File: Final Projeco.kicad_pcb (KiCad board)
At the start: 2 copper layers, 25 x 45 mm, 16 parts, among them U1 ESP32-S3, U2 GT-USB-7004N, U3 NCP167BMX330TBG, X1 TZ1269D

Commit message: Fixed all the traces to connect to each other :-|
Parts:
- added C8: 1uF, Capacitor_SMD:C_0402_1005Metric, F.Cu at (49.5, 56.5)
- added C9: 0.1uF, Capacitor_SMD:C_0402_1005Metric, F.Cu at (49.5, 59.0)
- added D1: SD103AWS_C5345966, jlc:SOD-323_L1.7-W1.3-LS2.5-RD, F.Cu at (35.2, 27.5)
- added D2: SD103AWS_C5345966, jlc:SOD-323_L1.7-W1.3-LS2.5-RD, F.Cu at (46.5, 24.7)
- added D3: SD103AWS_C5345966, jlc:SOD-323_L1.7-W1.3-LS2.5-RD, F.Cu at (44.5, 24.7)
- added R5: 100K, Resistor_SMD:R_0402_1005Metric, F.Cu at (47.0, 59.0)
- added U4: LY68L6400SLIT, jlc:SOP-8_L4.9-W3.9-P1.27-LS6.0-BL, F.Cu at (37.1, 33.7)
- added U5: PTS830GG140SMTRLFS, jlc:KEY-SMD_4P-L3.1-W2.6_PTS830GG140SMTRLFS, F.Cu at (43.9, 53.8)
- added U6: PTS830GG140SMTRLFS, jlc:KEY-SMD_4P-L3.1-W2.6_PTS830GG140SMTRLFS, F.Cu at (48.6, 53.8)
- added U7: 220S-2*16P_H=8_5MM_Ytype_L=3_0MM_PBT, jlc:HDR-TH_32P-P2.54-V-F-R2-C16-S2.54, F.Cu at (29.8, 36.6)
- C4: value C -> 1u
- moved U3 27.5 mm to (44.0, 17.0), turned to 90 degrees
- moved R1 18.3 mm to (41.0, 49.5), turned to 180 degrees
- moved U1 17.5 mm to (44.2, 33.9), turned to 180 degrees
- moved C7 13.3 mm to (47.0, 56.5), turned to 180 degrees
- moved X1 10.6 mm to (46.0, 40.1), turned to -90 degrees
- moved R2 10.5 mm to (40.9, 43.6)
- moved C2 10.5 mm to (38.0, 43.6)
- moved C3 10.5 mm to (38.0, 45.5)
- moved C4 10.5 mm to (38.0, 47.5)
- moved C5 10.5 mm to (38.0, 49.5)
- moved C6 10.5 mm to (38.0, 51.4)
- moved R3 10.5 mm to (40.9, 45.6), turned to 180 degrees
- moved R4 10.5 mm to (40.9, 47.6)
- moved C1 10.3 mm to (41.0, 41.0)
- moved U2 7.53 mm to (38.1, 21.9), turned to 180 degrees
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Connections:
- C1 pad 2: Net-(C1-Pad2) -> /XTAL_P
- C2 pad 1: Net-(C2-Pad1) -> /XTAL_N
- C3 pad 1: Net-(C3-Pad1) -> /RESET
- C5 pad 1: Net-(U3-OUT) -> VDD3P3
- C6 pad 1: Net-(U3-EN) -> /VBUS
- R1 pad 2: Net-(C3-Pad1) -> /RESET
- R2 pad 1: Net-(U2-CC2) -> /VBUS
- R3 pad 1: Net-(U2-CC1) -> /VBUS
- U1 pad 10: unconnected-(U1-GPIO5/ADC1_CH4-Pad10) -> /GPIO5
- U1 pad 11: unconnected-(U1-GPIO6/ADC1_CH5-Pad11) -> /GPIO6
- U1 pad 12: unconnected-(U1-GPIO7/ADC1_CH6-Pad12) -> /GPIO7
- U1 pad 13: unconnected-(U1-GPIO8/ADC1_CH7-Pad13) -> /GPIO8
- U1 pad 14: unconnected-(U1-GPIO9/ADC1_CH8-Pad14) -> /GPIO9'
- U1 pad 15: unconnected-(U1-GPIO10/ADC1_CH9-Pad15) -> /GPIO10
- U1 pad 16: unconnected-(U1-GPIO11/ADC2_CH0-Pad16) -> /GPIO11
- U1 pad 17: unconnected-(U1-GPIO12/ADC2_CH1-Pad17) -> /GPIO12
- U1 pad 18: unconnected-(U1-GPIO13/ADC2_CH2-Pad18) -> /GPIO13
- U1 pad 19: unconnected-(U1-GPIO14/ADC2_CH3-Pad19) -> /GPIO14
- U1 pad 20: unconnected-(U1-VDD3P3_RTC-Pad20) -> VDD3P3
- U1 pad 23: unconnected-(U1-GPIO17/ADC2_CH6-Pad23) -> /GPIO!7
- U1 pad 24: unconnected-(U1-GPIO18/ADC2_CH7-Pad24) -> /GPIO18
- U1 pad 25: unconnected-(U1-GPIO19/USB_D-/ADC2_CH8-Pad25) -> /USB_D+
- U1 pad 26: unconnected-(U1-GPIO20/USB_D+/ADC2_CH9-Pad26) -> /USB_D-
- U1 pad 27: unconnected-(U1-GPIO21-Pad27) -> /GPIO21
- U1 pad 28: unconnected-(U1-SPI_CS1/GPIO26-Pad28) -> /SPICS1
- U1 pad 29: unconnected-(U1-VDD_SPI-Pad29) -> VDD3P3
- U1 pad 30: unconnected-(U1-SPIHD/GPIO27-Pad30) -> /SPIHD
- U1 pad 31: unconnected-(U1-SPIWP/GPIO28-Pad31) -> /SPIWP
- U1 pad 33: unconnected-(U1-SPICLK/GPIO30-Pad33) -> /SPICLK
- U1 pad 34: unconnected-(U1-SPIQ/GPIO31-Pad34) -> /SPIQ
- U1 pad 35: unconnected-(U1-SPID/GPIO32-Pad35) -> /SPID
- U1 pad 4: unconnected-(U1-CHIP_PU/RESET-Pad4) -> /RESET
- U1 pad 43: unconnected-(U1-GPIO38-Pad43) -> /GPIO38
- U1 pad 46: unconnected-(U1-VDD3P3_CPU-Pad46) -> VDD3P3
- U1 pad 5: unconnected-(U1-GPIO0/BOOT-Pad5) -> /GPIO0/BOOT
- U1 pad 51: unconnected-(U1-GPIO45-Pad51) -> /GPIO45
- U1 pad 52: unconnected-(U1-GPIO46-Pad52) -> /GPIO46
- U1 pad 53: unconnected-(U1-XTAL_N-Pad53) -> /XTAL_P
- U1 pad 54: unconnected-(U1-XTAL_P-Pad54) -> /XTAL_N
- U1 pad 55: Net-(U1-VDDA-Pad55) -> VDD3P3
- U1 pad 56: Net-(U1-VDDA-Pad55) -> VDD3P3
- U1 pad 6: unconnected-(U1-GPIO1/ADC1_CH0-Pad6) -> /GPIO1
- U1 pad 7: unconnected-(U1-GPIO2/ADC1_CH1-Pad7) -> /GPIO2
- U1 pad 8: unconnected-(U1-GPIO3/ADC1_CH2-Pad8) -> /GPIO3
- U1 pad 9: unconnected-(U1-GPIO4/ADC1_CH3-Pad9) -> /GPIO4
- U2 pad 1: unconnected-(U2-SHELL-Pad1) -> GND
- U2 pad A4B9: Net-(U2-CC1) -> /VBUS
- U2 pad A5: Net-(U2-CC1) -> /VBUS
- U2 pad A6: unconnected-(U2-DP1-PadA6) -> /USB_D+
- U2 pad A7: unconnected-(U2-DN1-PadA7) -> /USB_D-
- U2 pad B4A9: Net-(U2-CC2) -> /VBUS
- U2 pad B5: Net-(U2-CC2) -> /VBUS
- U2 pad B6: unconnected-(U2-DP2-PadB6) -> /USB_D+
- U2 pad B7: unconnected-(U2-DN2-PadB7) -> /USB_D-
- U3 pad 1: Net-(U3-OUT) -> VDD3P3
- U3 pad 3: Net-(U3-EN) -> /VBUS
- U3 pad 4: Net-(U3-EN) -> /VBUS
- X1 pad 1: Net-(C1-Pad2) -> /XTAL_P
- X1 pad 3: Net-(C2-Pad1) -> /XTAL_N

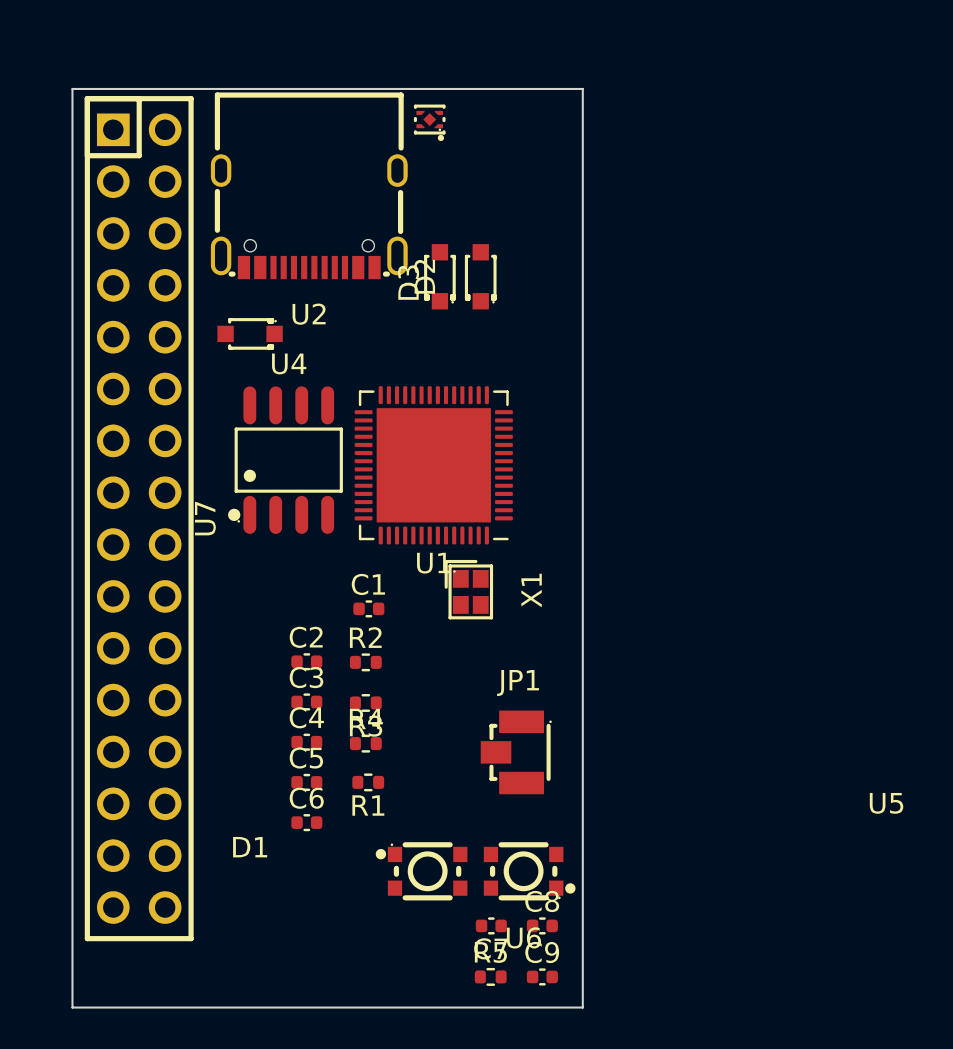
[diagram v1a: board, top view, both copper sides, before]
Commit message: Fixed some stuff
-added diff pair net rules
-added base net rules
-added zmatch net rules
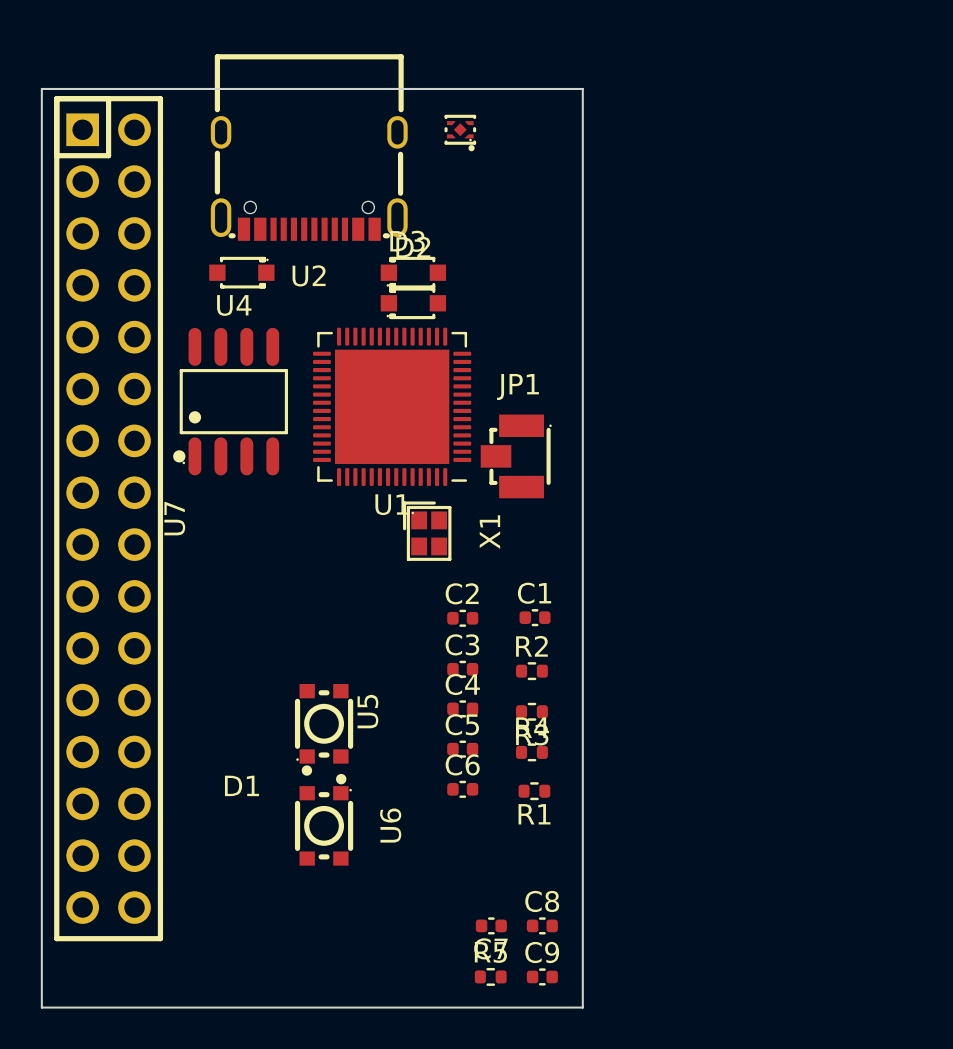
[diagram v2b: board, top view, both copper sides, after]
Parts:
- moved JP1 14.5 mm to (47.9, 33.5)
- moved U6 10.0 mm to (38.8, 51.6), turned to -90 degrees
- moved U5 8.83 mm to (38.8, 46.6), turned to 90 degrees
- moved R1 8.15 mm to (49.1, 49.9)
- moved R2 8.15 mm to (49.0, 44.0)
- moved R3 8.15 mm to (49.0, 46.0)
- moved R4 8.15 mm to (49.0, 48.0)
- moved C1 8.15 mm to (49.2, 41.4)
- moved C2 7.93 mm to (45.6, 41.4)
- moved C4 7.81 mm to (45.6, 45.9)
- moved C5 7.81 mm to (45.6, 47.8)
- moved C6 7.81 mm to (45.6, 49.8)
- moved C3 7.81 mm to (45.6, 43.9)
- moved U4 3.93 mm to (34.4, 30.8)
- moved D2 3.55 mm to (43.2, 26.0), turned to 0 degrees
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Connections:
- U1 pad 14: /GPIO9' -> /GPIO9
- U1 pad 23: /GPIO!7 -> /GPIO17
- U7 pad 11: unconnected-(U7-Pad11) -> /GPIO38
- U7 pad 12: /GPIO3 -> /GPIO4
- U7 pad 13: unconnected-(U7-Pad13) -> /GPIO45
- U7 pad 14: /GPIO4 -> /GPIO5
- U7 pad 15: unconnected-(U7-Pad15) -> /GPIO46
- U7 pad 16: /GPIO5 -> /GPIO6
- U7 pad 18: /GPIO6 -> /GPIO7
- U7 pad 20: /GPIO7 -> /GPIO8
- U7 pad 22: /GPIO8 -> /GPIO9
- U7 pad 24: /GPIO9' -> /GPIO10
- U7 pad 26: /GPIO10 -> /GPIO11
- U7 pad 28: /GPIO11 -> /GPIO12
- U7 pad 3: unconnected-(U7-Pad3) -> /GPIO14
- U7 pad 30: /GPIO12 -> /GPIO13
- U7 pad 31: unconnected-(U7-Pad31) -> VDD3P3
- U7 pad 32: /GPIO13 -> GND
- U7 pad 5: unconnected-(U7-Pad5) -> /GPIO17
- U7 pad 7: unconnected-(U7-Pad7) -> /GPIO18
- U7 pad 9: unconnected-(U7-Pad9) -> /GPIO21
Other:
- board size 25 x 45 mm -> 26.5 x 45 mm
- copper layers 2 -> 6

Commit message: Started Routing
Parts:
- C4: value 1u -> 1uF
- moved C6 30.2 mm to (43.9, 19.7)
- moved C5 28.3 mm to (48.6, 19.7), turned to 180 degrees
- moved R5 27.0 mm to (32.6, 36.2), turned to 90 degrees
- moved C9 25.0 mm to (33.3, 40.0)
- moved R3 24.6 mm to (47.0, 21.5), turned to -90 degrees
- moved R2 22.8 mm to (45.2, 21.5), turned to -90 degrees
- moved C8 22.0 mm to (33.3, 41.6)
- moved C4 20.3 mm to (48.4, 25.8)
- moved R1 13.7 mm to (37.5, 42.6)
- moved R4 10.3 mm to (40.2, 42.6)
- moved C3 9.56 mm to (38.1, 38.0)
- moved C1 9.32 mm to (40.5, 38.0)
- moved C7 7.32 mm to (41.6, 51.6), turned to 90 degrees
- moved D3 4.43 mm to (38.8, 25.0), turned to 180 degrees
- moved U3 3.20 mm to (48.7, 17.5)
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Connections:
- R1 pad 1: +3.3V -> VDD3P3
- R4 pad 1: +3.3V -> VDD3P3
- U1 pad 21: unconnected-(U1-GPIO15/ADC2_CH4/XTAL_32K_P-Pad21) -> /GPIO15
- U1 pad 22: unconnected-(U1-GPIO16/ADC2_CH5/XTAL_32K_N-Pad22) -> /GPIO16
- U1 pad 38: unconnected-(U1-GPIO33-Pad38) -> /GPIO33
- U1 pad 39: unconnected-(U1-GPIO34-Pad39) -> /GPIO34
- U1 pad 40: unconnected-(U1-GPIO35-Pad40) -> /GPIO35
- U1 pad 41: unconnected-(U1-GPIO36-Pad41) -> /GPIO36
- U1 pad 42: unconnected-(U1-GPIO37-Pad42) -> /GPIO37
- U7 pad 1: VDD3P3 -> /GPIO12
- U7 pad 10: /GPIO3 -> /GPIO2
- U7 pad 11: /GPIO38 -> /GPIO17
- U7 pad 12: /GPIO4 -> /GPIO3
- U7 pad 13: /GPIO45 -> /GPIO18
- U7 pad 14: /GPIO5 -> /GPIO4
- U7 pad 15: /GPIO46 -> /GPIO21
- U7 pad 16: /GPIO6 -> /GPIO5
- U7 pad 17: unconnected-(U7-Pad17) -> /GPIO38
- U7 pad 18: /GPIO7 -> /GPIO6
- U7 pad 19: unconnected-(U7-Pad19) -> /GPIO45
- U7 pad 20: /GPIO8 -> /GPIO7
- U7 pad 21: unconnected-(U7-Pad21) -> /GPIO46
- U7 pad 22: /GPIO9 -> /GPIO8
- U7 pad 23: unconnected-(U7-Pad23) -> /GPIO33
- U7 pad 24: /GPIO10 -> /GPIO9
- U7 pad 25: unconnected-(U7-Pad25) -> /GPIO34
- U7 pad 26: /GPIO11 -> /GPIO10
- U7 pad 27: unconnected-(U7-Pad27) -> /GPIO35
- U7 pad 28: /GPIO12 -> /GPIO11
- U7 pad 29: unconnected-(U7-Pad29) -> /GPIO36
- U7 pad 3: /GPIO14 -> /GPIO13
- U7 pad 30: /GPIO13 -> VDD3P3
- U7 pad 31: VDD3P3 -> /GPIO37
- U7 pad 4: /GPIO0/BOOT -> VDD3P3
- U7 pad 5: /GPIO17 -> /GPIO14
- U7 pad 6: /GPIO1 -> /GPIO0/BOOT
- U7 pad 7: /GPIO18 -> /GPIO15
- U7 pad 8: /GPIO2 -> /GPIO1
- U7 pad 9: /GPIO21 -> /GPIO16
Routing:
- net /VBUS: track 0.00 -> 29.0 mm
- net GND: track 0.00 -> 23.2 mm, vias 0 -> 19
- net VDD3P3: track 0.00 -> 11.0 mm, vias 0 -> 8
- net /USB_D+: track 0.00 -> 9.45 mm, vias 0 -> 2
- net /USB_D-: track 0.00 -> 9.03 mm
- net /XTAL_N: track 0.00 -> 7.91 mm
- net /XTAL_P: track 0.00 -> 6.53 mm
- net Net-(JP1-SIN): track 0.00 -> 1.90 mm
- net /RESET: track 0.00 -> 1.31 mm
- added copper zone on In1.Cu, net GND
- added copper zone on In2.Cu, net VDD3P3
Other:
- board text added: "William Schoon"

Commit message: stuff
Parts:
- added C10: 1uF, Capacitor_SMD:C_0402_1005Metric, F.Cu at (35.5, 36.3)
- added R6: 442k, Resistor_SMD:R_0402_1005Metric, F.Cu at (37.4, 36.3)
- C1, C2: value C -> 13pF
- C5, C6: value C -> 1uF
- moved C4 2.33 mm to (47.2, 27.8)
- moved U7 0.59 mm to (28.5, 37.1)
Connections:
- net Net-(U1-GND) renamed /GND_PIN
- U1 pad 37: unconnected-(U1-SPICLK_P/GPIO47-Pad37) -> /SPICLK_GPIO47
- U2 pad 2: unconnected-(U2-SHELL-Pad2) -> GND
- U2 pad 3: unconnected-(U2-SHELL-Pad3) -> GND
- U2 pad 4: unconnected-(U2-SHELL-Pad4) -> GND
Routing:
- net /GND_PIN: track 0.00 -> 5.96 mm
- net VDD3P3: track 11.0 -> 13.9 mm
- net /USB_D-: track 9.03 -> 9.92 mm
- net GND: track 23.2 -> 23.8 mm

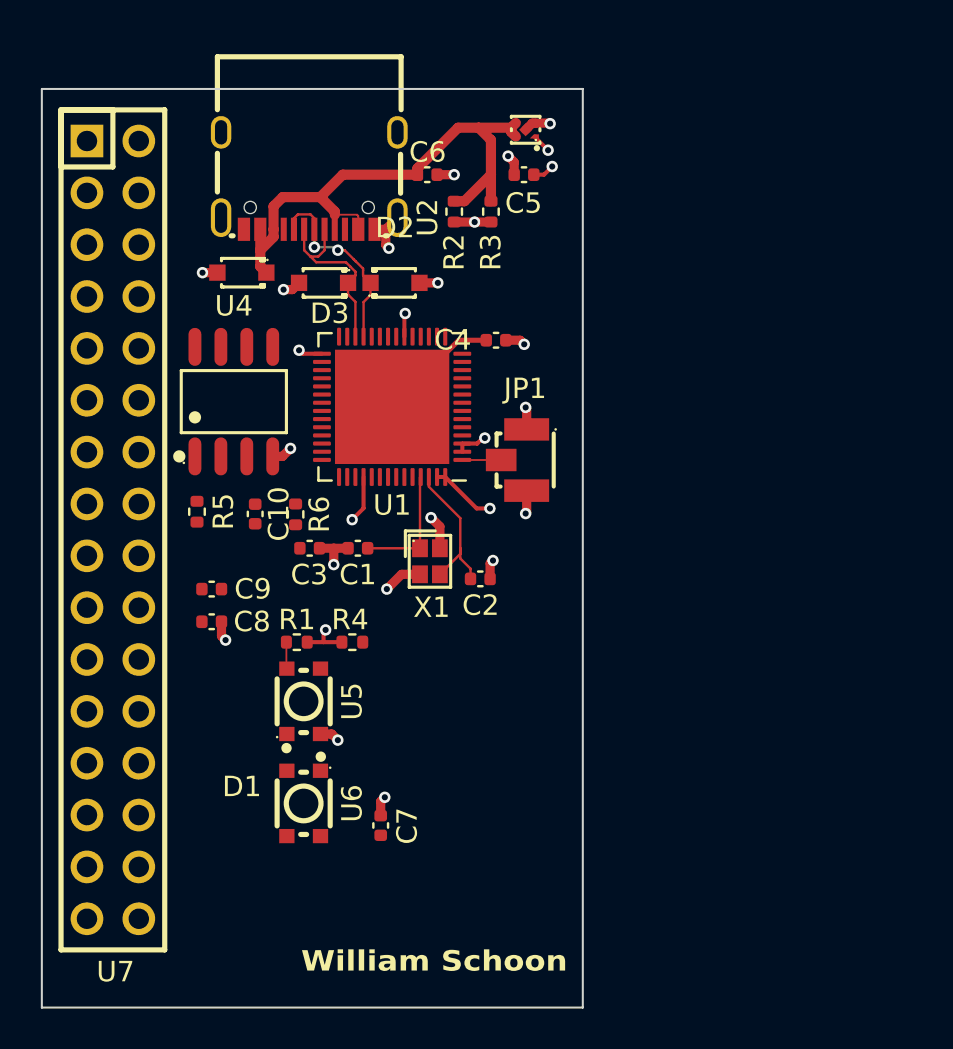
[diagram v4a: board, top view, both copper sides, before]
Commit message: Final build init commit
-No DRC errors,
-All routed
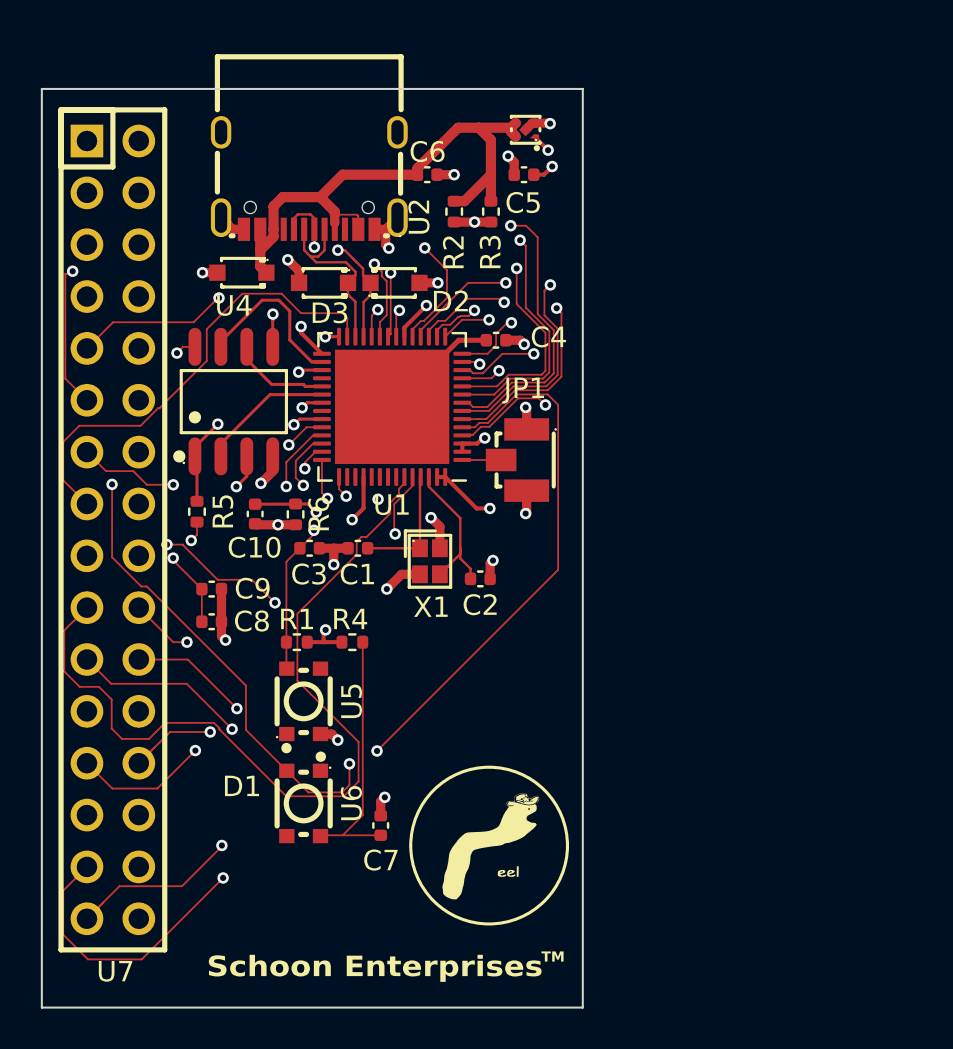
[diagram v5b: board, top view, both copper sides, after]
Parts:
- added G***: LOGO, Schoon:small_front_monochrome, F.Cu at (47.4, 52.6)
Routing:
- net /GPIO0/BOOT: track 0.00 -> 69.0 mm, vias 0 -> 3
- net /GPIO6: track 0.00 -> 59.9 mm, vias 0 -> 1
- net /GPIO9: track 0.00 -> 49.4 mm, vias 0 -> 1
- net /GPIO7: track 0.00 -> 42.1 mm, vias 0 -> 2
- net /GPIO45: track 0.00 -> 40.8 mm
- net /GPIO2: track 0.00 -> 40.5 mm, vias 0 -> 1
- net /GPIO36: track 0.00 -> 39.5 mm, vias 0 -> 2
- net /GPIO13: track 0.00 -> 39.2 mm, vias 0 -> 1
- net /GPIO1: track 0.00 -> 39.0 mm, vias 0 -> 1
- net /GPIO8: track 0.00 -> 36.4 mm, vias 0 -> 2
- net /GPIO3: track 0.00 -> 36.4 mm, vias 0 -> 1
- net /GPIO5: track 0.00 -> 35.2 mm, vias 0 -> 1
- net /GPIO4: track 0.00 -> 35.1 mm, vias 0 -> 1
- net /GPIO11: track 0.00 -> 35.0 mm, vias 0 -> 1
- net /GPIO14: track 0.00 -> 34.8 mm, vias 0 -> 1
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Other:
- board text added: "Schoon Enterprises"
- board text added: "TM"
- board text removed: "William Schoon"
